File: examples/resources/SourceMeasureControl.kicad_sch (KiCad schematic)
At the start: 11 parts

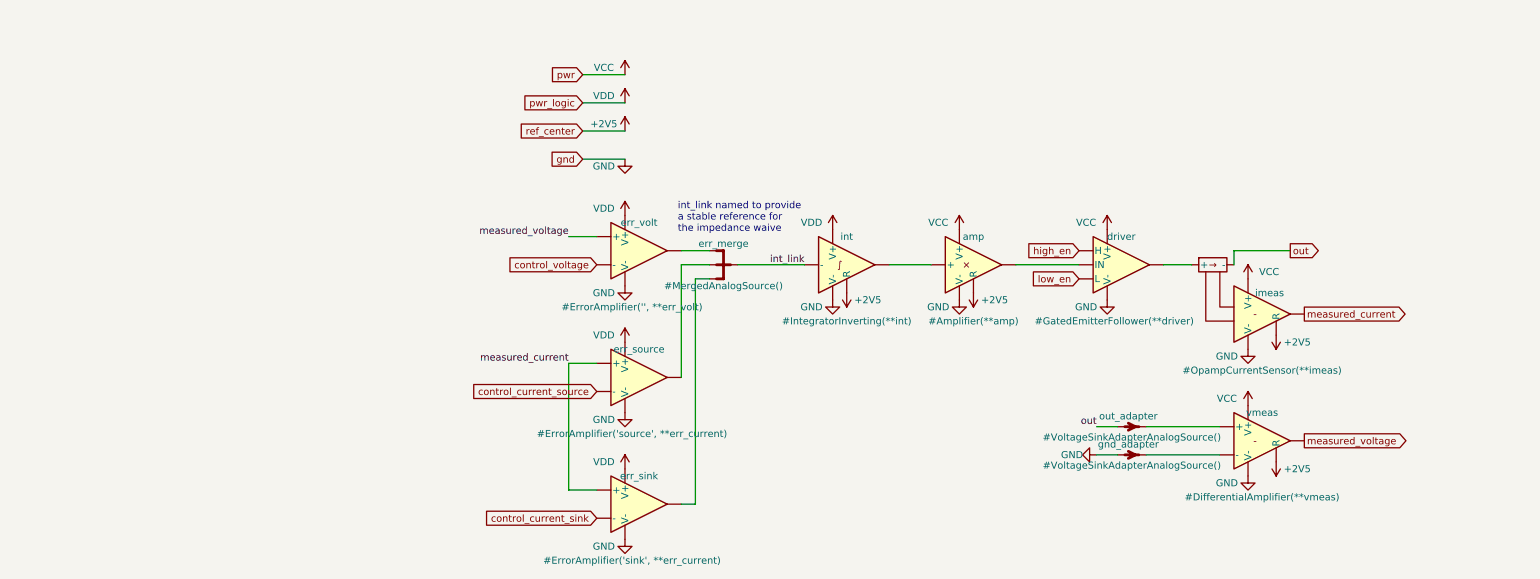
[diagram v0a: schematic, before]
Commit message: finalize the stricter checking
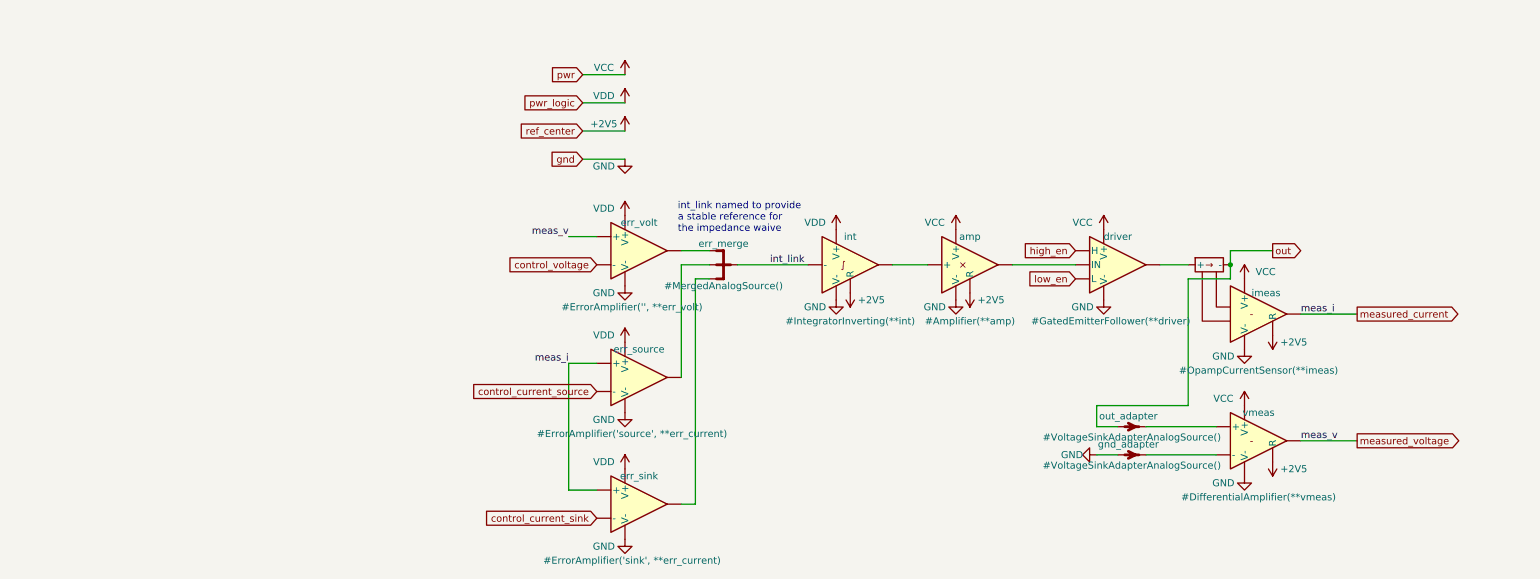
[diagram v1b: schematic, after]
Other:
- moved on the sheet: amp, driver, imeas, int, vmeas

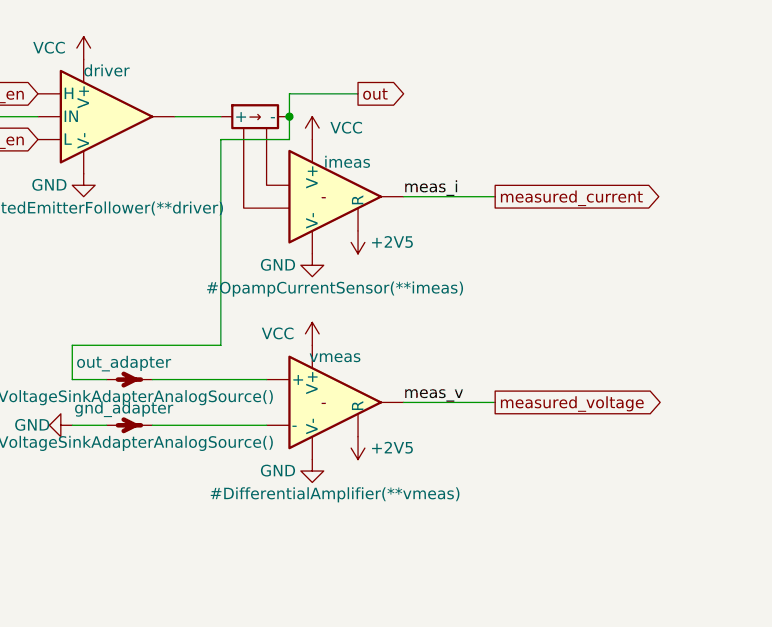
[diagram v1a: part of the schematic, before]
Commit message: fix SMU w/ zener diode
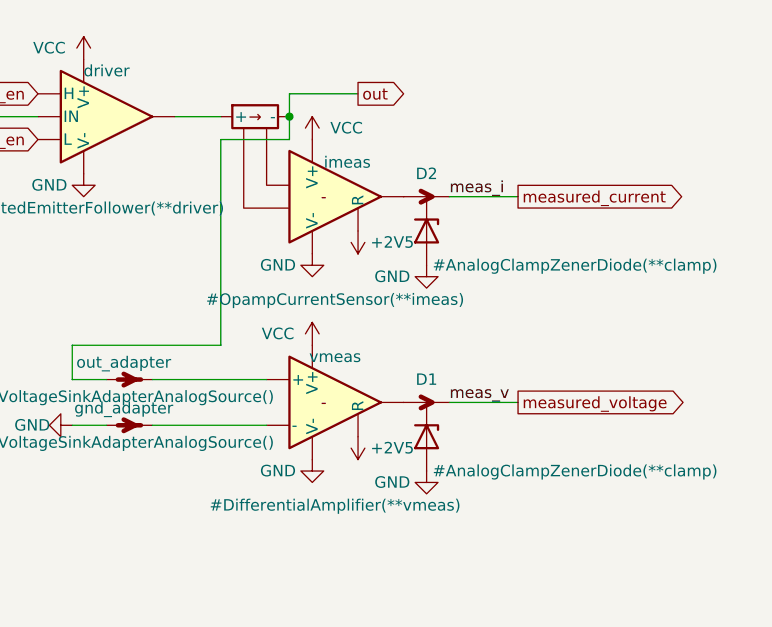
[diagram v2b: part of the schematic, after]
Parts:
- added D1, D2: #AnalogClampZenerDiode(**clamp), symbol edg_importable:AnalogClampZenerDiode
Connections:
- net GND: now also D1.3 (GND), D2.3 (GND)
- net measured_current: now also D2.2 (OUT); no longer imeas.3
- net measured_voltage: now also D1.2 (OUT); no longer vmeas.3
- new net: D1.1 (IN), vmeas.3
- new net: D2.1 (IN), imeas.3

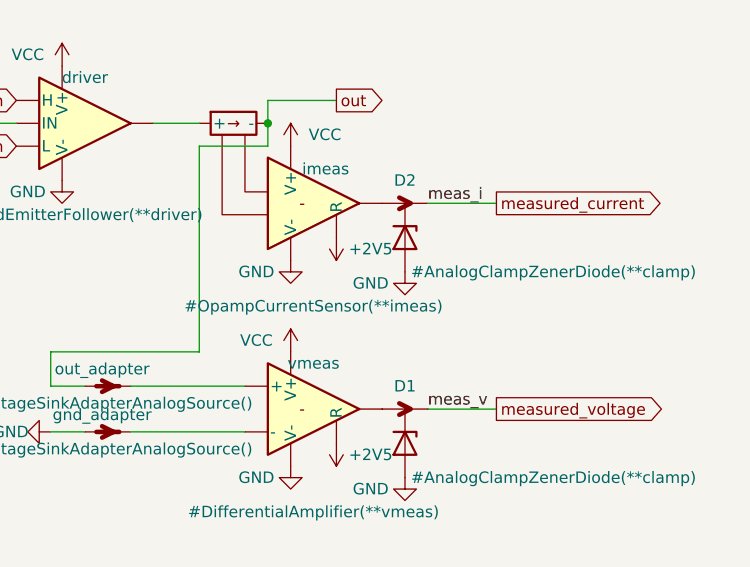
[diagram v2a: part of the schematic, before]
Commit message: SMU clamp diode
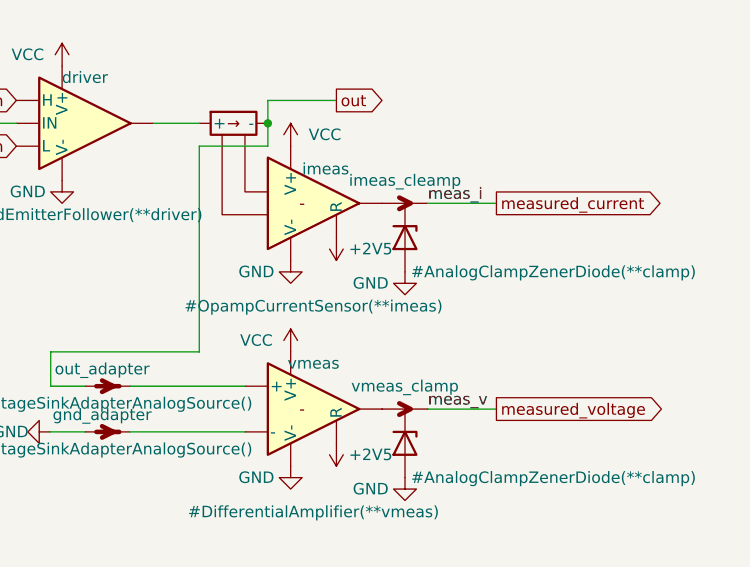
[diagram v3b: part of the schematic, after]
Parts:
- renumbered D2 to imeas_cleamp, D1 to vmeas_clamp
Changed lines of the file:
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@@
   (symbol (lib_id "edg_importable:AnalogClampZenerDiode") (at 248.92 127 0) (unit 1)
     (in_bom yes) (on_board yes) (dnp no)
-    (property "Reference" "D1" (at 248.92 120.65 0)
+    (property "Reference" "vmeas_clamp" (at 248.92 120.65 0)
       (effects (font (size 1.27 1.27)))
     )
@@
       (project "SourceMeasureControl"
         (path "/b55f6c44-5d5d-4524-bb86-893662f64598"
-          (reference "D1") (unit 1)
+          (reference "vmeas_clamp") (unit 1)
         )
       )
@@
   (symbol (lib_id "edg_importable:AnalogClampZenerDiode") (at 248.92 104.14 0) (unit 1)
     (in_bom yes) (on_board yes) (dnp no)
-    (property "Reference" "D2" (at 248.92 97.79 0)
+    (property "Reference" "imeas_cleamp" (at 248.92 97.79 0)
       (effects (font (size 1.27 1.27)))
     )
@@
       (project "SourceMeasureControl"
         (path "/b55f6c44-5d5d-4524-bb86-893662f64598"
-          (reference "D2") (unit 1)
-        )
-      )
+          (reference "imeas_cleamp") (unit 1)
+        )
+      )

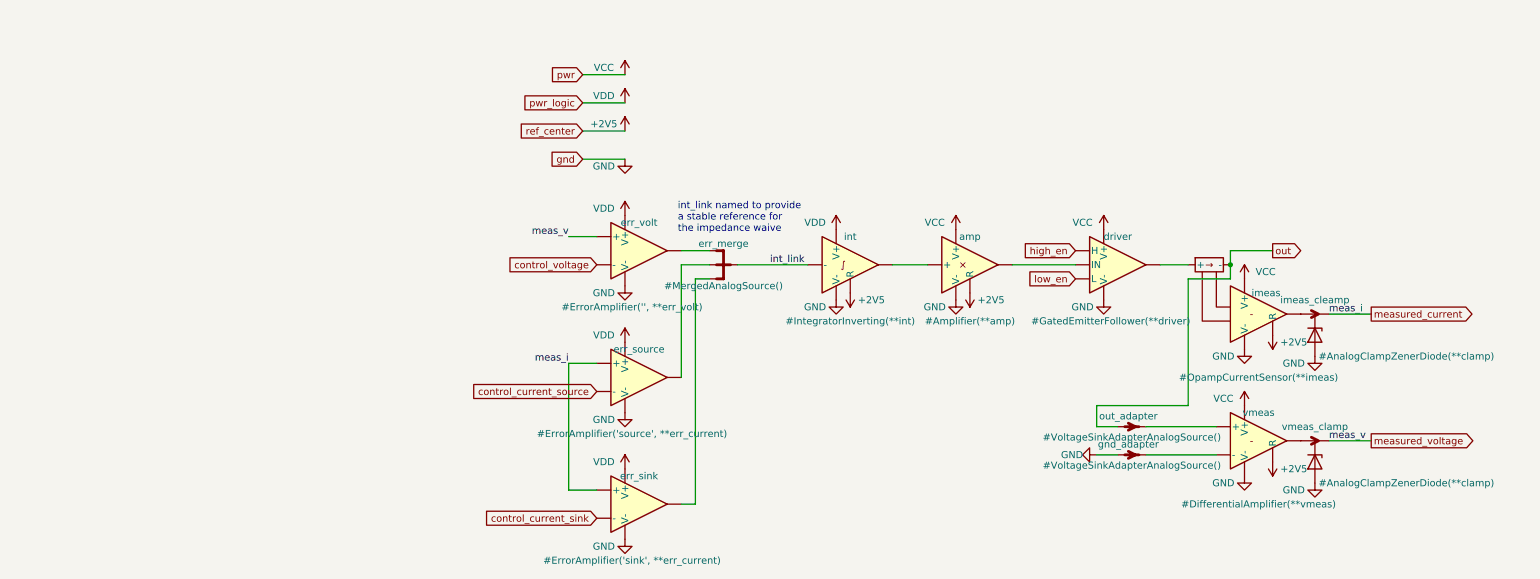
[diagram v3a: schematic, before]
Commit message: USB SMU v2 (#310)
Update for the USB SMU example device
- Emitter follower - add zener-based gate clamping circuit
- Change on/off control to use a SSR on the output (instead of on the
control line) - in preparation for a future current ranging circuit
- Unify data and power USB into one connector
- Add test points
- Add buck-boost converter preregulator
- Primary rail is 6v (instead of 5v) - to power the gate driver
- Add bootstrap voltage adder to provide gate power for linear stage
- Add OLED, encoder, directional switch
- Use MCP4728 DAC, MCP3561 ADC - higher resolution than what was before
- Use multipack OPA2197 opamps for high volt amps

Infrastructural changes
- BoM generator: also generate manufacturer and part

Library changes:
- Fix a long-standing capacitor table error where floating inaccuracy
causes it to over-aggressively filter rows
- Improve capacitor parsing, filter JLC caps by >X5R
- FETs: default to zero gate voltage (for Vgs,max purposes)
- Buck-boost power path: switch ports now Passive, actual current
ratings moved into separate parameters
- Add VoltageIsolatedSwitch, a SSR for VoltageSource/VoltageSink
- Add TLP3545A high current SSR
- Add DirectionSwitch (a switch with four directions),
DirectionSwitchCenter mixin, Digital* wrappers, Alps SKRH series
directional switches (with footprint)
- Clean up inverting integrator opamp RC, make component calculations
more straightforward
- Allow MCP3561 without VRef
- Add bootstrap voltage adder (switched cap voltage adder) -
EXPERIMENTAL
- Add CustomSyncBuckBoostConverter
- Add MCP4728 12-bit DAC, MCP47Fx DACs (unused - pricey)
- Add TMP1075N temperature sensor
- Add PCA9554 I2C IO expander in TSSOP16
- Add I2C address to PCF8574
- Add dual-packed OPA2197
- Add PEC11S rotary encoder (with footprint, slightly different from the
EC15 series)
- Make duckling symbol board-only, made ref on symbol footprints on Fab
layer
- Add prerouted blocks
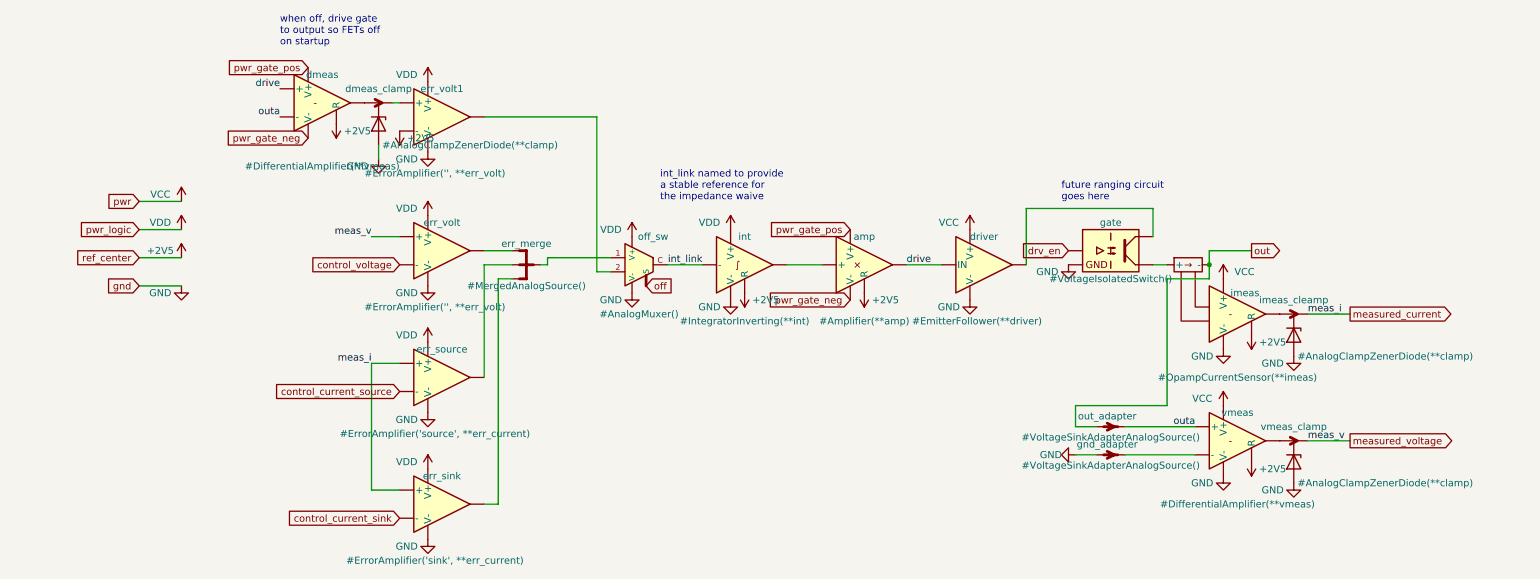
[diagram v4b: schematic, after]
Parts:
- added dmeas: #DifferentialAmplifier(**vmeas), symbol edg_importable:DifferentialAmplifier
- added dmeas_clamp: #AnalogClampZenerDiode(**clamp), symbol edg_importable:AnalogClampZenerDiode
- added err_volt1: #ErrorAmplifier('', **err_volt), symbol edg_importable:Opamp
- added gate: #VoltageIsolatedSwitch(), symbol edg_importable:VoltageIsolatedSwitch
- added off_sw: #AnalogMuxer(), symbol edg_importable:Mux2
- driver: value #GatedEmitterFollower(**driver) -> #EmitterFollower(**driver)
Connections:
- net +2V5: now also dmeas.6 (R), err_volt1.2 (-)
- net GND: now also dmeas_clamp.3 (GND), err_volt1.5 (V-), gate.2 (gnd), off_sw. (V-); no longer amp.5 (V-)
- net VCC: no longer amp.4 (V+)
- net VDD: now also err_volt1.4 (V+), off_sw. (V-)
- net int_link: now also off_sw.C; no longer err_merge.0
- net outa: now reaches out_adapter.2, vmeas.1 (+)
- net outa: now also dmeas.2 (-)
- net drive: now reaches amp.3, driver.1 (IN)
- net drive: now also dmeas.1 (+)
- net at driver.3: now also gate.4 (ain); no longer imeas.1 (+)
- removed net high_en: driver.6 (H)
- removed net low_en: driver.7 (L)
- new net: dmeas.3, dmeas_clamp.1 (IN)
- new net: err_merge.0, off_sw.1
- new net: err_volt1.3, off_sw.2
- new net: dmeas_clamp.2 (OUT), err_volt1.1 (+)
- new net: gate.3 (aout), imeas.1 (+)
- new net drv_en: gate.1 (in)
- new net off: off_sw. (V-)
- new net pwr_gate_neg: amp.5 (V-), dmeas.5 (V-)
- new net pwr_gate_pos: amp.4 (V+), dmeas.4 (V+)
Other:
- note added: "future ranging circuit goes here"
- note added: "when off, drive gate to output so FETs off on startup"
- moved on the sheet: amp, err_merge, err_sink, err_source, err_volt, gnd_adapter, imeas, imeas_cleamp, int, out_adapter, vmeas, vmeas_clamp

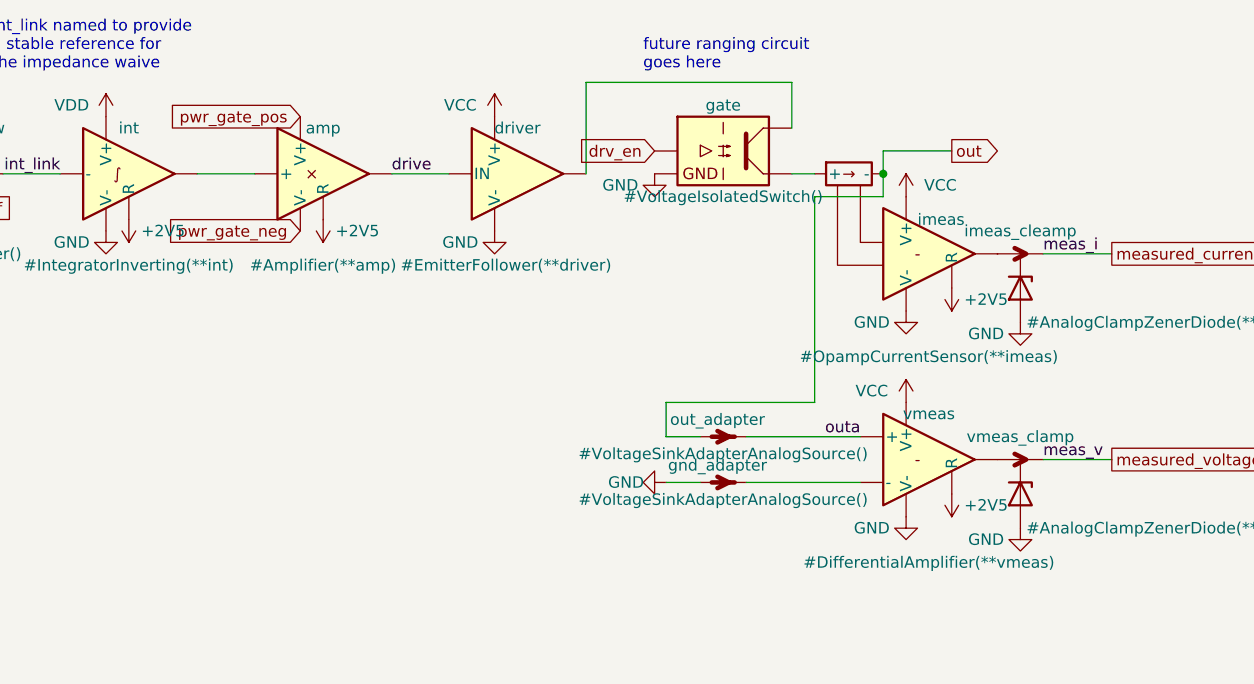
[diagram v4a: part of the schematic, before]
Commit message: ad8418a current sense amp + add bufferamp
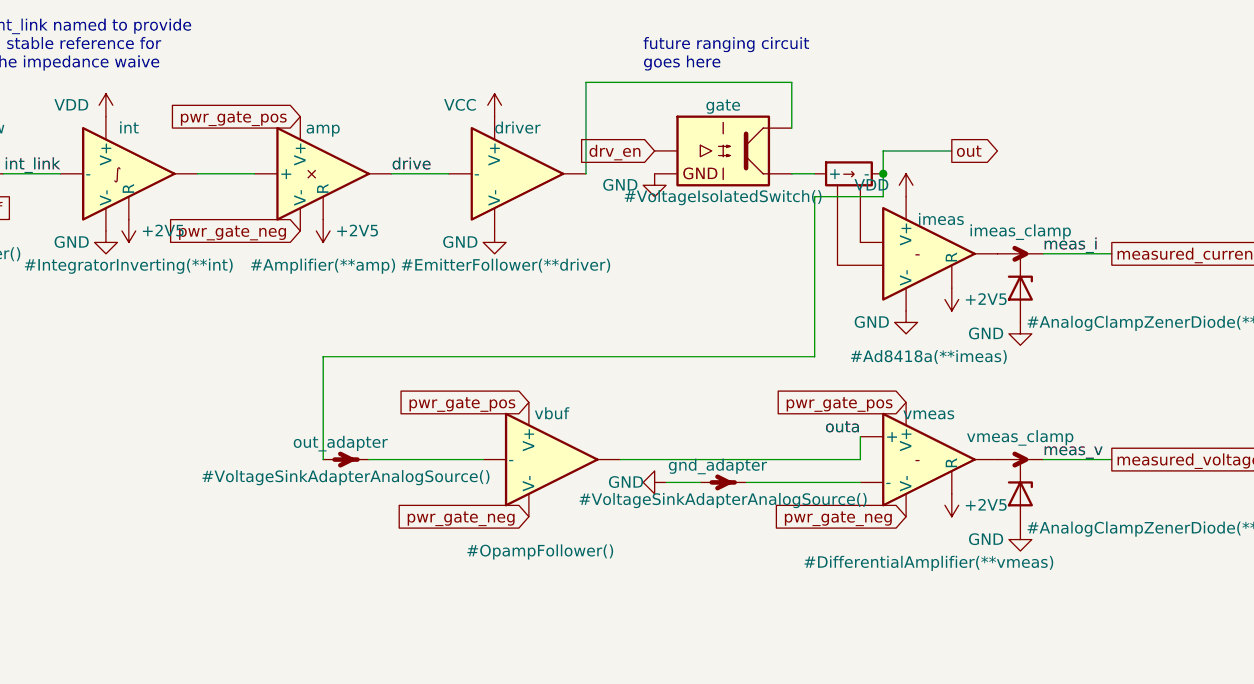
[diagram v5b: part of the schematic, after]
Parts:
- added vbuf: #OpampFollower(), symbol edg_importable:Follower
- driver: symbol edg_importable:Opamp -> edg_importable:Follower
- imeas: value #OpampCurrentSensor(**imeas) -> #Ad8418a(**imeas)
- renumbered imeas_cleamp to imeas_clamp
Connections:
- net GND: no longer vmeas.5 (V-)
- net VCC: no longer imeas.4 (V+), vmeas.4 (V+)
- net VDD: now also imeas.4 (V+)
- net outa: now also vbuf.3; no longer out_adapter.2
- net pwr_gate_neg: now also vmeas.5 (V-), vbuf.5 (V-)
- net pwr_gate_pos: now also vmeas.4 (V+), vbuf.4 (V+)
- new net: out_adapter.2, vbuf.1 (-)
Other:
- moved on the sheet: out_adapter

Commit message: wip clamp dev
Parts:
- removed dmeas_clamp, imeas_clamp, vmeas_clamp: #AnalogClampZenerDiode(**clamp), symbol edg_importable:AnalogClampZenerDiode
- added dclamp, vclamp: #AnalogClampResistor(**clamp), symbol Device:R
- added inclamp: #AnalogClampResistor(clamp_target=(0, 30)*Volt, p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, symbol Device:R
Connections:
- net measured_current: now also imeas.3
- net measured_voltage: now also vclamp.2
- net at dmeas.3: now also dclamp.1
- net at vmeas.3: now also vclamp.1
- net at out_adapter.2: now also inclamp.1; no longer vbuf.1 (-)
- net at err_volt1.1 (+): now also dclamp.2
- new net: inclamp.2, vbuf.1 (-)
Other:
- moved on the sheet: dmeas, out_adapter

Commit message: progress
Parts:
- added dbuf, vbuf: #OpampFollower(), symbol edg_importable:Follower
- renumbered err_volt1 to err_d, vbuf to hvbuf, inclamp to hvclamp
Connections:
- net GND: now also dbuf.5 (V-), vbuf.5 (V-)
- net VDD: now also dbuf.4 (V+), vbuf.4 (V+)
- net measured_voltage: now also vbuf.1; no longer err_volt.1 (+)
- net at err_d.1 (+): now also dbuf.3; no longer dclamp.2
- new net: dbuf.1, dclamp.2
- new net meas_v: err_volt.1 (+), vbuf.3
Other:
- moved on the sheet: dclamp, dmeas, hvclamp, out_adapter
